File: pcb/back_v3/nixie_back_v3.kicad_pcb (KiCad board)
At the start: 2 copper layers, 110 x 50 mm, 26 parts, among them J1 UART, J2 BUTTONS, J3 LED, J4 POWER, J5 LEFT, J6 RIGHT, SW1 BOOT, SW2 RESET, U1 DS3231MZ, U2 ESP32-WROOM-E

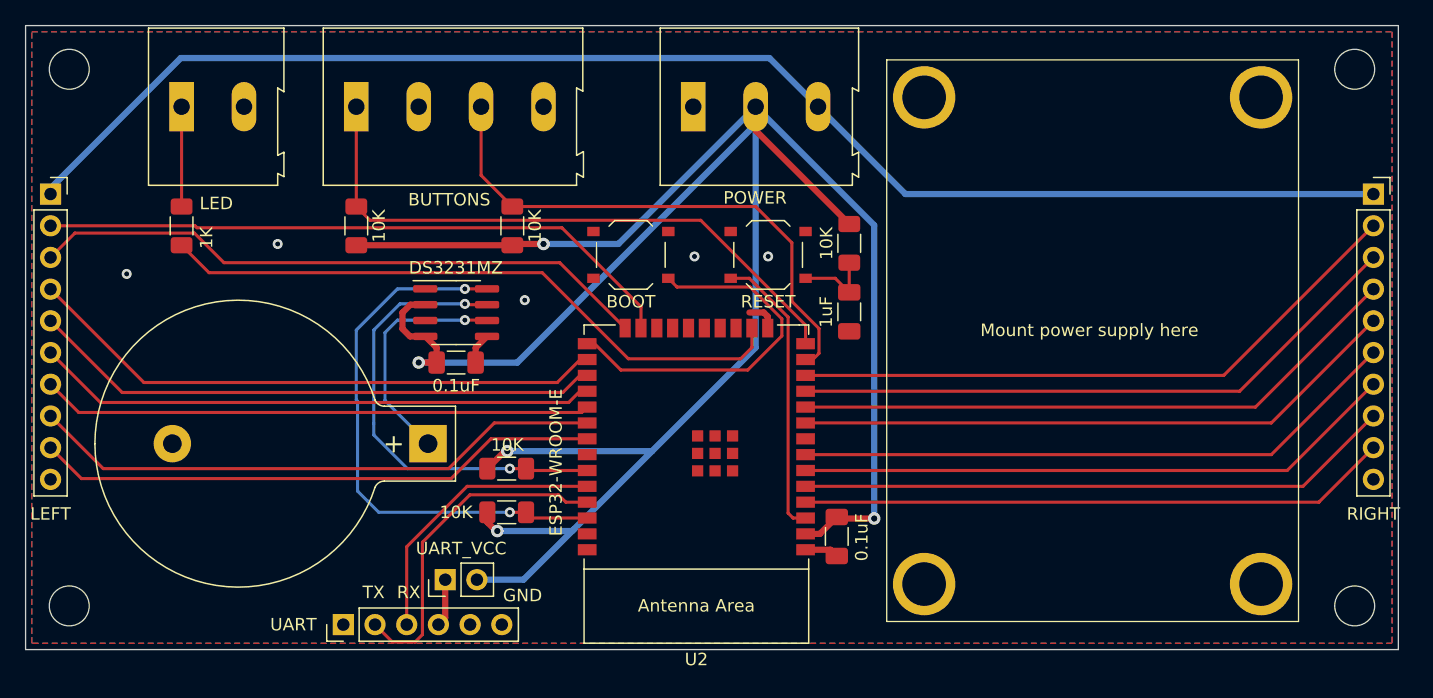
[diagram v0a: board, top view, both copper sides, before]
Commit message: Rename kicad project
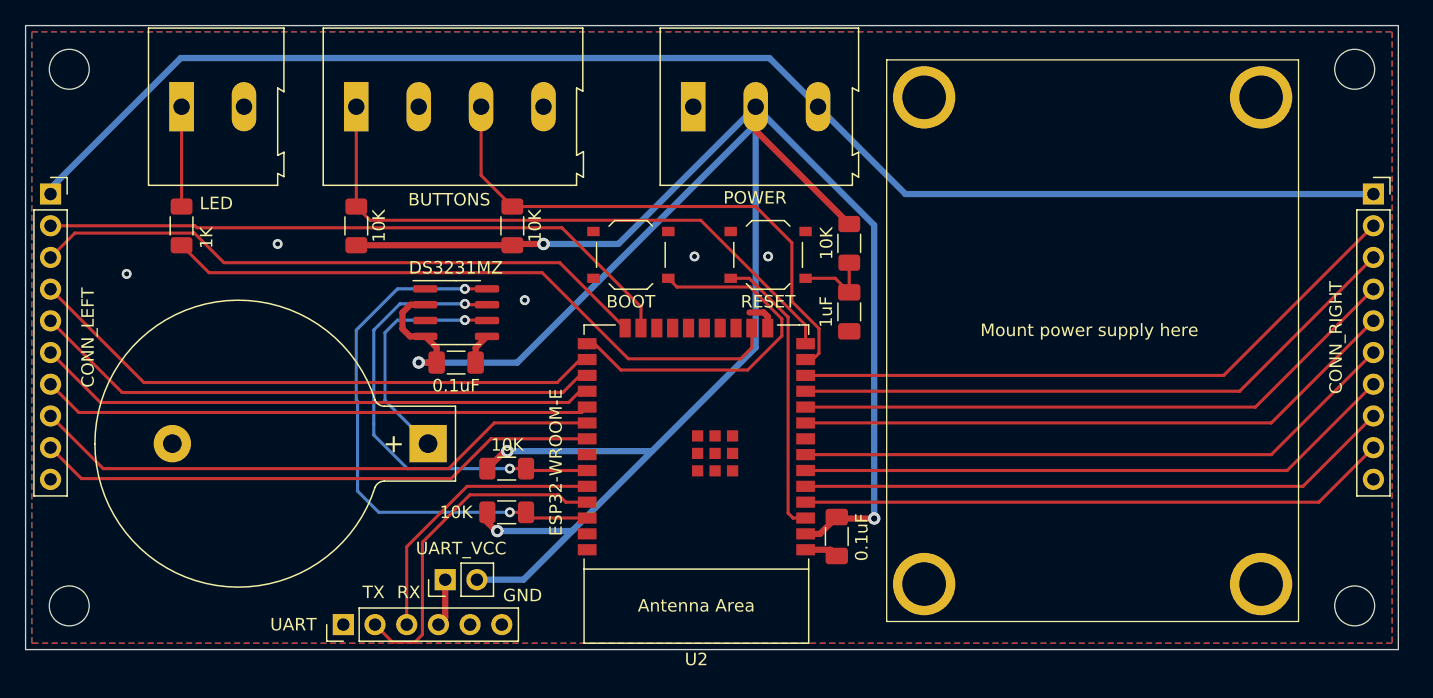
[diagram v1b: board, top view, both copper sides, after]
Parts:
- J5: value LEFT -> CONN_LEFT
- J6: value RIGHT -> CONN_RIGHT
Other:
- board text added: "Nixie Clock Back Panel v3.0 Ilya Strukov, 2023"
- board text added: "This side towards front panel"
- board text removed: "Nixie Clock Back Panel v2.0 Ilya Strukov, 2023"
